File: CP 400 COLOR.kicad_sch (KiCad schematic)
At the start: 167 parts, among them CN1 CN9, CN10 CN10, CN13 CN13, CN14 CN14, CN2 CASSETE, CN3 CN8, CN4 RS232, CN5 JOYESQ, CN6 JOYDIR, CN8 CN12

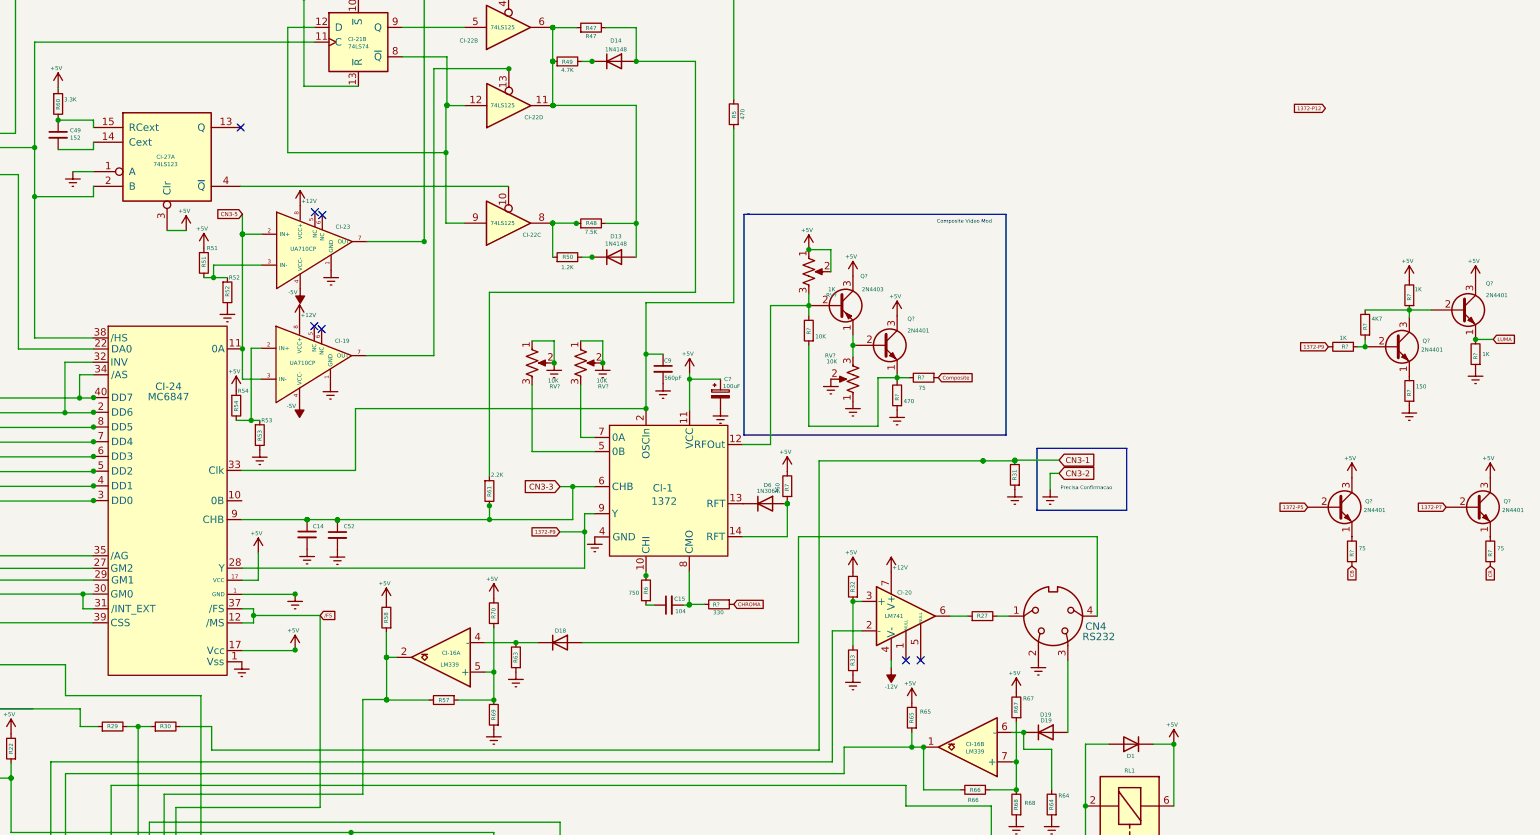
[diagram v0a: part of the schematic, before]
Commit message: Added video mod to the schematic - removed RF circuit
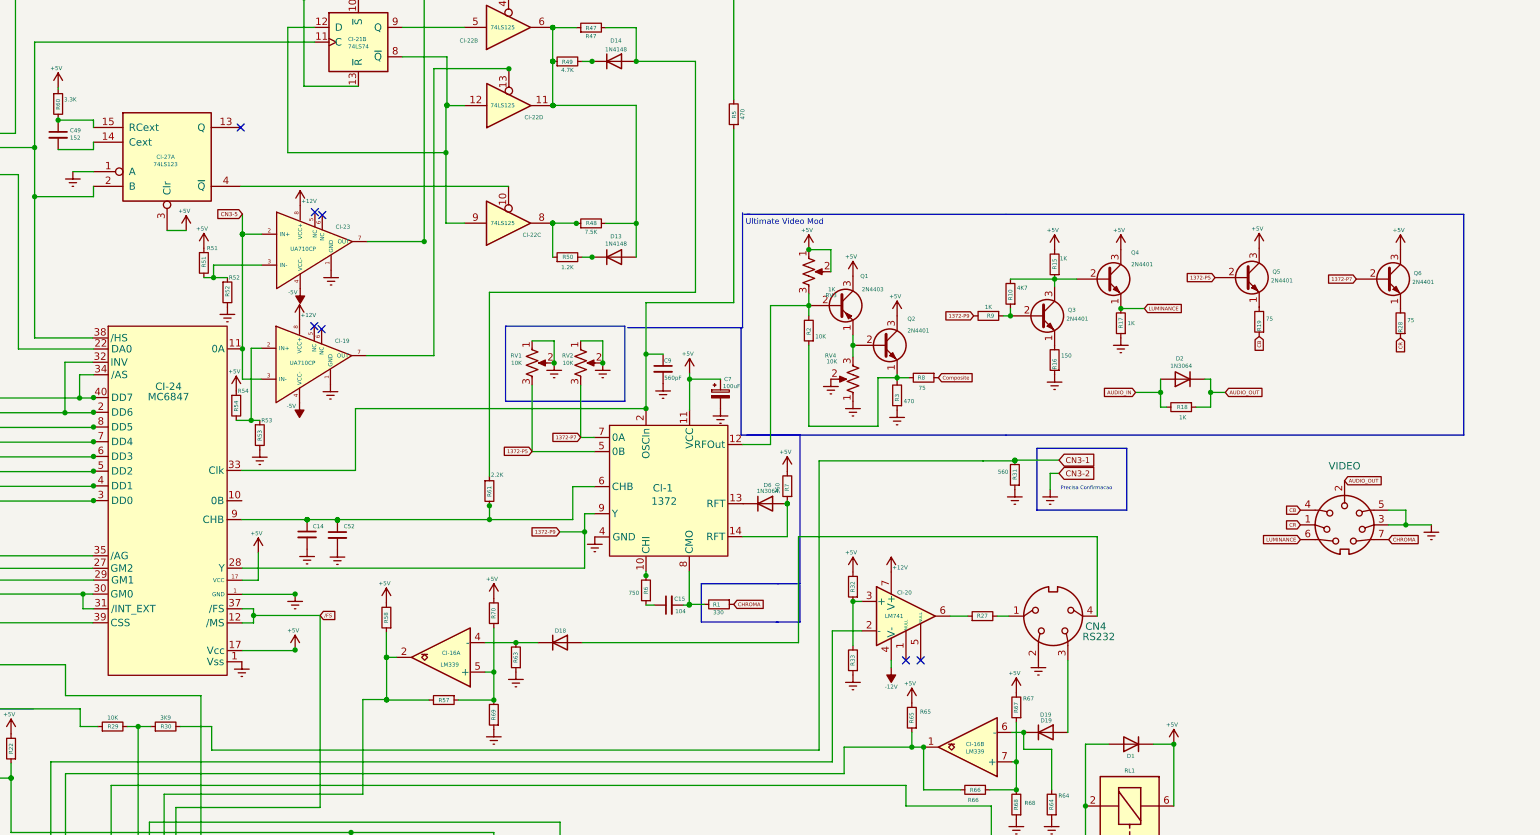
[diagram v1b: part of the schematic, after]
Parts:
- added D2: 1N3064, Diode_THT:D_DO-34_SOD68_P7.62mm_Horizontal, symbol Diode:1N4148W
- added J1: VIDEO, symbol Connector:DIN-7
- added R18: 1K, Resistor_THT:R_Axial_DIN0207_L6.3mm_D2.5mm_P7.62mm_Horizontal, symbol Device:R_Small
- R29: value R29 -> 10K
- R30: value R30 -> 3K9
- R31: value R31 -> 560
- gave numbers to parts that had none: 21
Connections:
- net 1372-P5: now also CI-1.5 (0B), RV1.3
- net 1372-P7: now also CI-1.7 (0A), RV2.3
- net CB: now also J1.4
- net CHROMA: now also J1.7
- net CR: now also J1.1
- net GNDREF: now also J1.3, J1.5
- net CN3-3: no longer names the net of C14.1, C52.1, CI-1.6 (CHB), CI-24.9 (CHB), R61.2
- net LUMA renamed LUMINANCE
- net LUMINANCE: now also J1.6
- new net AUDIO_IN: D2.2 (A), R18.2
- new net AUDIO_OUT: D2.1 (K), J1.2, R18.1
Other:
- note added: "Ultimate Video Mod"
- note removed: "Composite Video Mod"
- moved on the sheet: Q3, Q4, Q5, Q6, R10, R15, R16, R17, R19, R28, R9

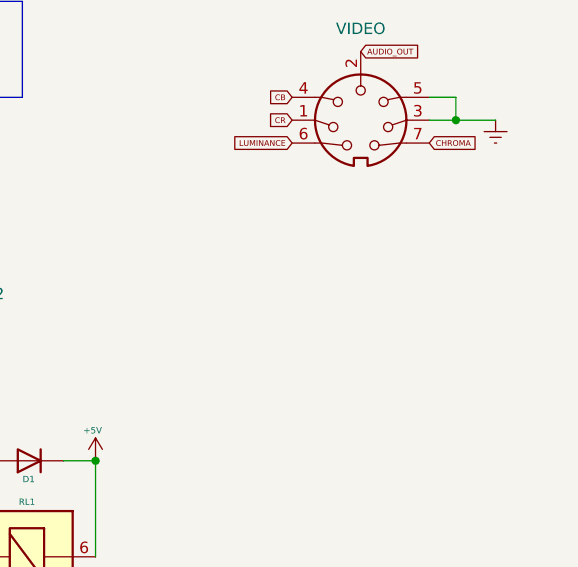
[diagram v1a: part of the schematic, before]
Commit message: Added coaxial connector for composite video
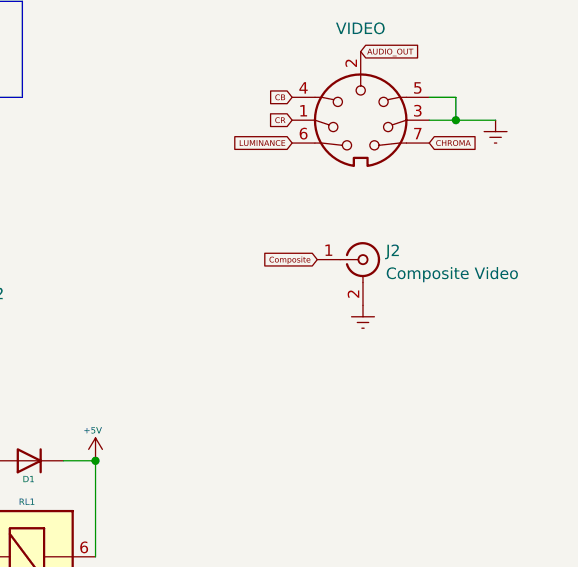
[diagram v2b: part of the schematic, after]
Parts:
- added J2: Composite Video, symbol Connector:Conn_Coaxial
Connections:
- net Composite: now also J2.1 (In)
- net GNDREF: now also J2.2 (Ext)
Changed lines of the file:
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@@
   (title_block
     (title "CP 400 COLOR 2 - PROLOGICA 12 REV.3")
-    (date "2022-12-13")
+    (date "2023-02-09")
     (rev "0.3")
     (company "PROLOGICA")
@@
     )
   )
+  (global_label "Composite" (shape input) (at 521.97 135.89 180) (fields_autoplaced)
+    (effects (font (size 0.635 0.635)) (justify right))
+    (property "Intersheet References" "${INTERSHEET_REFS}" (id 0) (at 515.8346 135.9297 0)
+      (effects (font (size 0.635 0.635)) (justify right) hide)
+    )
+  )
   (global_label "CNI14-9" (shape input) (at 333.6526 279.7763 0) (fields_autoplaced)
     (effects (font (size 1 1)) (justify left))
@@
     (pin "2")
   )
+  (symbol (lib_id "power:GNDREF") (at 527.05 140.97 0) (unit 1)
+    (in_bom yes) (on_board yes) (fields_autoplaced)
+    (property "Reference" "#PWR023" (id 0) (at 527.05 147.32 0)
+      (effects (font (size 0.7 0.7)) hide)
+    )
+    (property "Value" "GNDREF" (id 1) (at 527.05 145.542 0)
+      (effects (font (size 0.7 0.7)) hide)
+    )
+    (property "Footprint" "" (id 2) (at 527.05 140.97 0)
+      (effects (font (size 0.7 0.7)) hide)
+    )
+    (property "Datasheet" "" (id 3) (at 527.05 140.97 0)
+      (effects (font (size 0.7 0.7)) hide)
+    )
+    (pin "1")
+  )
   (symbol (lib_id "power:+5V") (at 234.442 369.062 180) (unit 1)
     (in_bom yes) (on_board yes)
@@
     (pin "1")
   )
+  (symbol (lib_id "Connector:Conn_Coaxial") (at 527.05 135.89 0) (unit 1)
+    (in_bom yes) (on_board yes) (fields_autoplaced)
+    (property "Reference" "J2" (id 0) (at 529.59 134.9131 0)
+      (effects (font (size 1.27 1.27)) (justify left))
+    )
+    (property "Value" "Composite Video" (id 1) (at 529.59 137.4531 0)
+      (effects (font (size 1.27 1.27)) (justify left))
+    )
+    (property "Footprint" "" (id 2) (at 527.05 135.89 0)
+      (effects (font (size 1.27 1.27)) hide)
+    )
+    (property "Datasheet" " ~" (id 3) (at 527.05 135.89 0)
+      (effects (font (size 1.27 1.27)) hide)
+    )
+    (pin "1")
+    (pin "2")
+  )
   (symbol (lib_id "Device:C_Small") (at 116.84 156.718 0) (unit 1)
     (in_bom yes) (on_board yes)
@@
   (symbol (lib_id "power:GNDREF") (at 541.782 120.396 0) (unit 1)
     (in_bom yes) (on_board yes) (fields_autoplaced)
-    (property "Reference" "#PWR?" (id 0) (at 541.782 126.746 0)
+    (property "Reference" "#PWR024" (id 0) (at 541.782 126.746 0)
       (effects (font (size 0.7 0.7)) hide)
     )
@@
       (reference "#PWR022") (unit 1) (value "+5V") (footprint "")
     )
+    (path "/2b9246de-d1da-4966-bc4a-123ab6dad563"
+      (reference "#PWR023") (unit 1) (value "GNDREF") (footprint "")
+    )
+    (path "/719bac72-789c-498b-8898-281901c76c8b"
+      (reference "#PWR024") (unit 1) (value "GNDREF") (footprint "")
+    )
     (path "/cdaf8996-5dbd-47e8-8244-07b97717e380"
       (reference "#PWR0101") (unit 1) (value "+5V") (footprint "")
@@
       (reference "#PWR0256") (unit 1) (value "+5V") (footprint "")
     )
-    (path "/719bac72-789c-498b-8898-281901c76c8b"
-      (reference "#PWR?") (unit 1) (value "GNDREF") (footprint "")
-    )
     (path "/75eb4e97-453b-4950-ab62-f4387fca9a8d"
       (reference "C1") (unit 1) (value "223") (footprint "Capacitor_THT:C_Axial_L3.8mm_D2.6mm_P7.50mm_Horizontal")
@@
       (reference "J1") (unit 1) (value "VIDEO") (footprint "")
     )
+    (path "/4a6ef9f3-5485-45c2-a6a8-eecb41c9b5a6"
+      (reference "J2") (unit 1) (value "Composite Video") (footprint "")
+    )
     (path "/39b9e0c1-8bd3-4611-ba25-2b662abe6420"

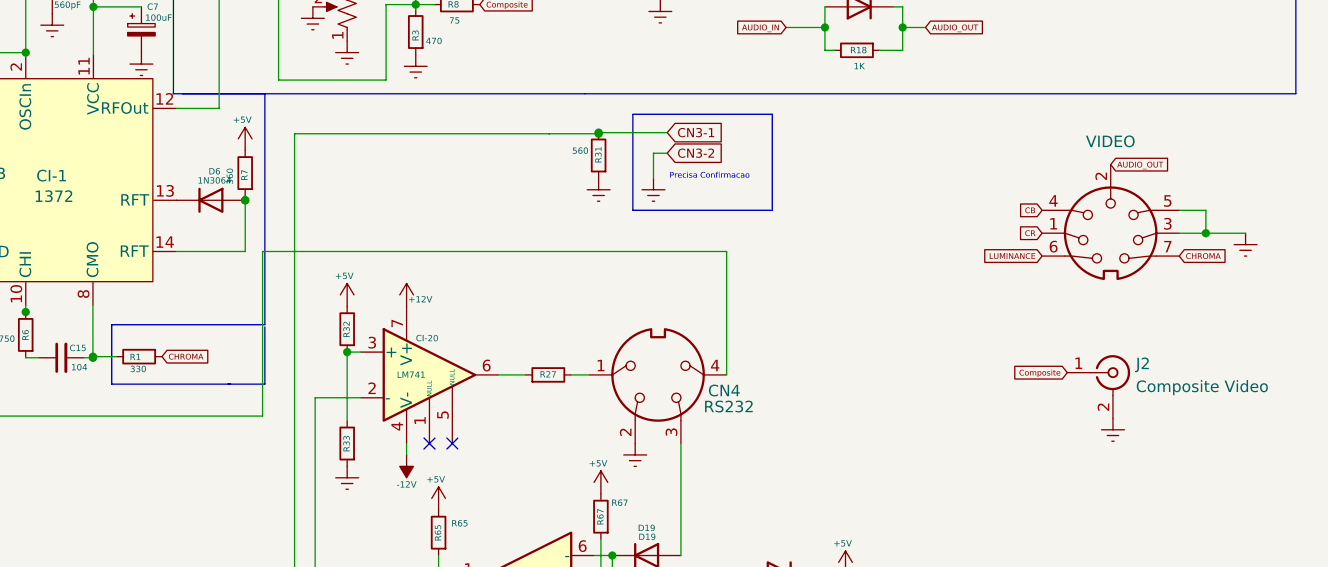
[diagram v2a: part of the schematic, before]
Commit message: changed pinout of din-7 for compatibility with cable in datassete.org
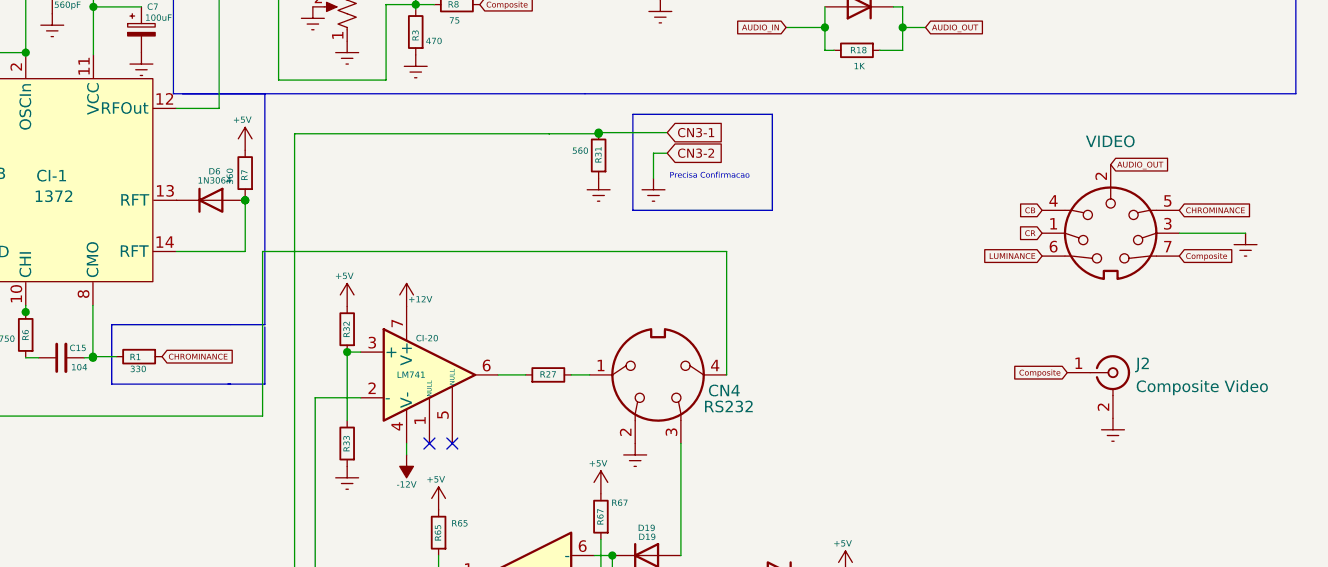
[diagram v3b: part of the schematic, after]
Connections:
- net Composite: now also J1.7
- net GNDREF: no longer J1.5
- net CHROMA renamed CHROMINANCE
- net CHROMINANCE: now also J1.5; no longer J1.7
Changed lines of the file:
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@@
   (junction (at 148.717 128.9812) (diameter 0) (color 0 0 0 0)
   )
-  (junction (at 537.3708 120.396) (diameter 0) (color 0 0 0 0)
-  )
   (junction (at 361.4805 150.5339) (diameter 0) (color 0 0 0 0)
   )
@@
     (stroke (width 0) (type default) (color 0 0 0 0))
   )
-  (wire (pts (xy 537.3708 120.396) (xy 541.782 120.396))
-    (stroke (width 0) (type default) (color 0 0 0 0))
-  )
   (wire (pts (xy 263.652 67.818) (xy 263.652 70.612))
     (stroke (width 0) (type default) (color 0 0 0 0))
@@
     (stroke (width 0) (type default) (color 0 0 0 0))
   )
-  (wire (pts (xy 537.3708 117.856) (xy 537.3708 120.396))
-    (stroke (width 0) (type default) (color 0 0 0 0))
-  )
   (wire (pts (xy 390.398 88.646) (xy 390.398 92.456))
     (stroke (width 0) (type default) (color 0 0 0 0))
@@
     (stroke (width 0) (type default) (color 0 0 0 0))
   )
-  (wire (pts (xy 534.416 120.396) (xy 537.3708 120.396))
+  (wire (pts (xy 534.416 120.396) (xy 541.782 120.396))
     (stroke (width 0) (type default) (color 0 0 0 0))
   )
@@
     (stroke (width 0) (type default) (color 0 0 0 0))
   )
-  (wire (pts (xy 534.416 117.856) (xy 537.3708 117.856))
-    (stroke (width 0) (type default) (color 0 0 0 0))
-  )
   (wire (pts (xy 484.124 122.428) (xy 432.562 122.428))
     (stroke (width 0) (type default) (color 0 0 0 0))
@@
     )
   )
+  (global_label "Composite" (shape input) (at 534.416 122.936 0) (fields_autoplaced)
+    (effects (font (size 0.635 0.635)) (justify left))
+    (property "Intersheet References" "${INTERSHEET_REFS}" (id 0) (at 540.5514 122.8963 0)
+      (effects (font (size 0.635 0.635)) (justify left) hide)
+    )
+  )
   (global_label "CB" (shape input) (at 512.064 87.884 270) (fields_autoplaced)
     (effects (font (size 0.635 0.635)) (justify right))
@@
     )
   )
-  (global_label "CHROMA" (shape input) (at 534.416 122.936 0) (fields_autoplaced)
+  (global_label "CHROMINANCE" (shape input) (at 534.416 117.856 0) (fields_autoplaced)
     (effects (font (size 0.635 0.635)) (justify left))
-    (property "Intersheet References" "${INTERSHEET_REFS}" (id 0) (at 539.4931 122.8963 0)
+    (property "Intersheet References" "${INTERSHEET_REFS}" (id 0) (at 542.3355 117.8163 0)
       (effects (font (size 0.635 0.635)) (justify left) hide)
     )
@@
     )
   )
-  (global_label "CHROMA" (shape input) (at 421.386 134.112 0) (fields_autoplaced)
+  (global_label "CHROMINANCE" (shape input) (at 421.386 134.112 0) (fields_autoplaced)
     (effects (font (size 0.635 0.635)) (justify left))
-    (property "Intersheet References" "${INTERSHEET_REFS}" (id 0) (at 426.4631 134.0723 0)
+    (property "Intersheet References" "${INTERSHEET_REFS}" (id 0) (at 429.3055 134.0723 0)
       (effects (font (size 0.635 0.635)) (justify left) hide)
     )
